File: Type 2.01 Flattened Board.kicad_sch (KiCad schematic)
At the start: 7 parts

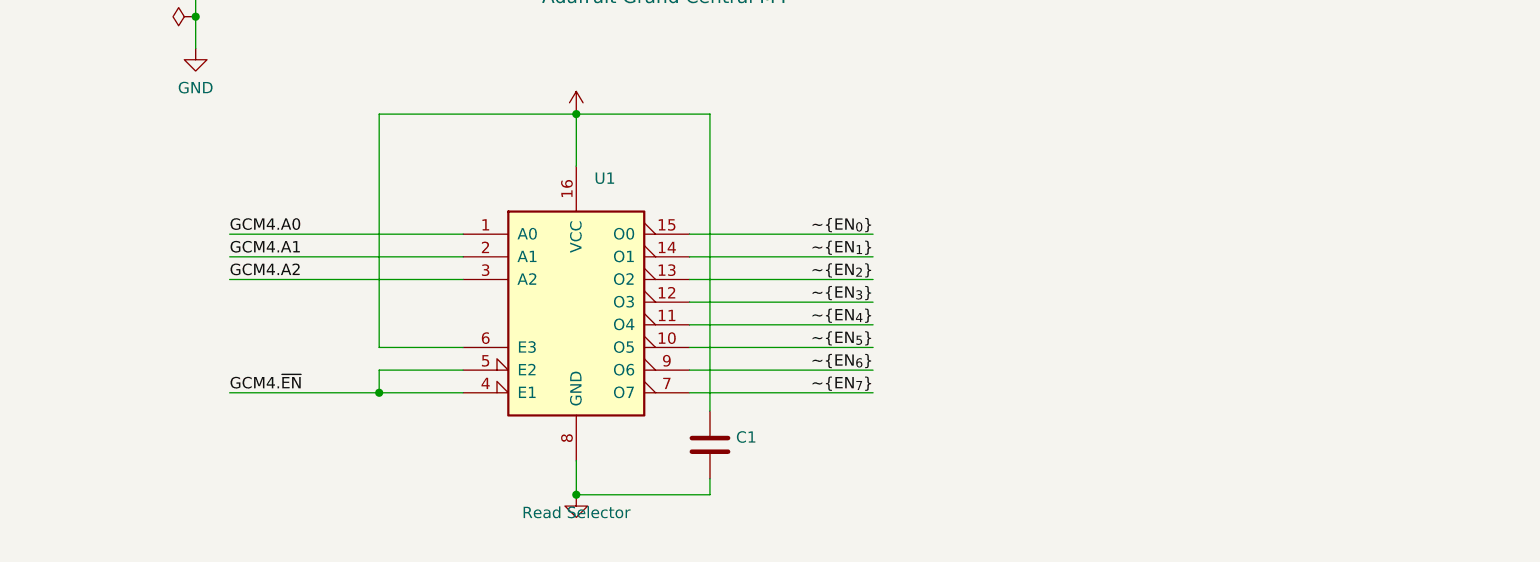
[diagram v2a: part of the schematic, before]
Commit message: Added the LOW global label
Simplify things
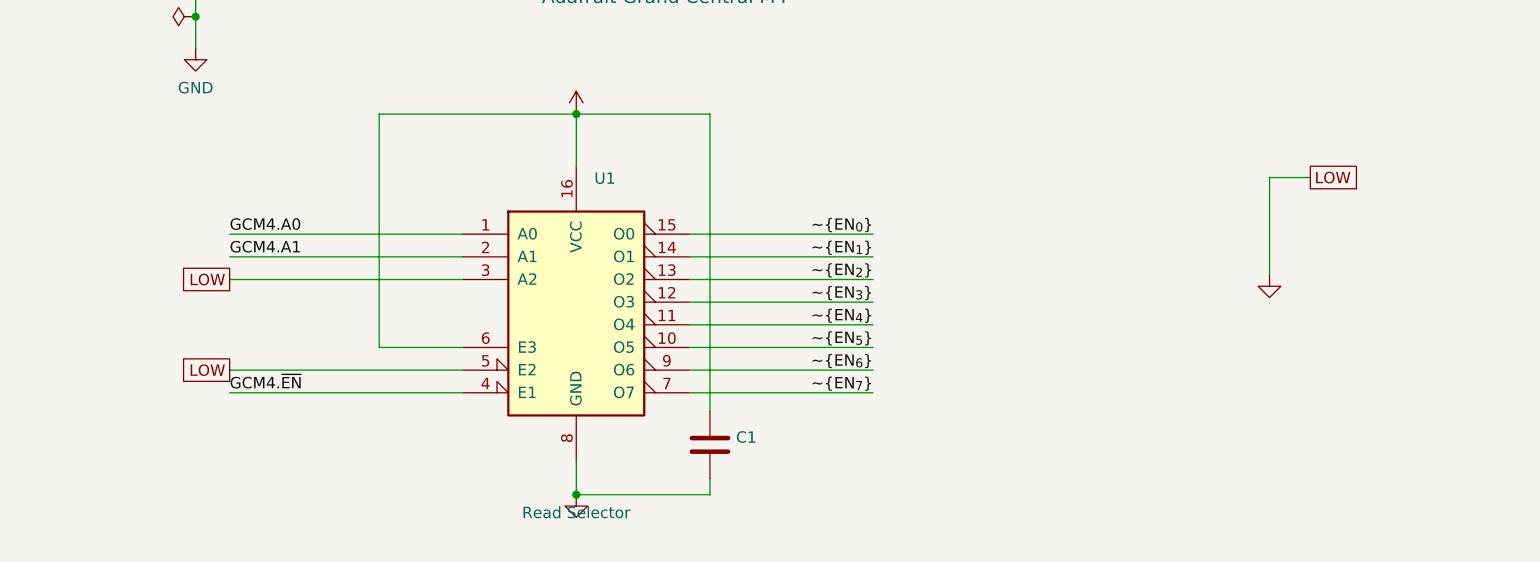
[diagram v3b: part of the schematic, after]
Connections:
- net GCM4.A2 is gone; now on net GND: U1.3 (A2)
- net BUS.PA23: no longer U1.5 (E2)
- net GND: now also U1.5 (E2)
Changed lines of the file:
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@@
   (junction (at 54.102 193.548) (diameter 0) (color 0 0 0 0)
   )
-  (junction (at 74.676 235.712) (diameter 0) (color 0 0 0 0)
-  )
   (junction (at 130.302 16.51) (diameter 0) (color 0 0 0 0)
   )
@@
     (stroke (width 0) (type default) (color 0 0 0 0))
   )
+  (wire (pts (xy 179.07 211.582) (xy 174.498 211.582))
+    (stroke (width 0) (type default) (color 0 0 0 0))
+  )
   (wire (pts (xy 139.7 159.512) (xy 187.452 159.512))
     (stroke (width 0) (type default) (color 0 0 0 0))
@@
     (stroke (width 0) (type default) (color 0 0 0 0))
   )
-  (wire (pts (xy 57.912 235.712) (xy 74.676 235.712))
+  (wire (pts (xy 174.498 211.582) (xy 174.498 222.504))
+    (stroke (width 0) (type default) (color 0 0 0 0))
+  )
+  (wire (pts (xy 57.912 235.712) (xy 84.074 235.712))
     (stroke (width 0) (type default) (color 0 0 0 0))
   )
@@
     (stroke (width 0) (type default) (color 0 0 0 0))
   )
-  (wire (pts (xy 84.074 233.172) (xy 74.676 233.172))
+  (wire (pts (xy 57.912 233.172) (xy 84.074 233.172))
     (stroke (width 0) (type default) (color 0 0 0 0))
   )
@@
     (stroke (width 0) (type default) (color 0 0 0 0))
   )
-  (wire (pts (xy 74.676 235.712) (xy 84.074 235.712))
-    (stroke (width 0) (type default) (color 0 0 0 0))
-  )
   (wire (pts (xy 84.074 230.632) (xy 74.676 230.632))
     (stroke (width 0) (type default) (color 0 0 0 0))
@@
     (stroke (width 0) (type default) (color 0 0 0 0))
   )
-  (wire (pts (xy 74.676 233.172) (xy 74.676 235.712))
-    (stroke (width 0) (type default) (color 0 0 0 0))
-  )
   (bus (pts (xy 313.436 181.61) (xy 313.436 160.274))
     (stroke (width 0) (type default) (color 0 0 0 0))
@@
     (effects (font (size 1.27 1.27)) (justify left bottom))
   )
-  (label "GCM4.A2" (at 57.912 223.012 0)
-    (effects (font (size 1.27 1.27)) (justify left bottom))
-  )
   (label "BUS.PA2" (at 61.214 106.172 0)
     (effects (font (size 1.27 1.27)) (justify left bottom))
@@
     (effects (font (size 1.27 1.27)) (justify right bottom))
   )
+  (global_label "LOW" (shape passive) (at 179.07 211.582 0) (fields_autoplaced)
+    (effects (font (size 1.27 1.27)) (justify left))
+    (property "Intersheet References" "${INTERSHEET_REFS}" (id 0) (at 185.2042 211.5026 0)
+      (effects (font (size 1.27 1.27)) (justify left) hide)
+    )
+  )
+  (global_label "LOW" (shape passive) (at 57.912 233.172 180) (fields_autoplaced)
+    (effects (font (size 1.27 1.27)) (justify right))
+    (property "Intersheet References" "${INTERSHEET_REFS}" (id 0) (at 51.7778 233.2514 0)
+      (effects (font (size 1.27 1.27)) (justify right) hide)
+    )
+  )
+  (global_label "LOW" (shape passive) (at 57.912 223.012 180) (fields_autoplaced)
+    (effects (font (size 1.27 1.27)) (justify right))
+    (property "Intersheet References" "${INTERSHEET_REFS}" (id 0) (at 51.7778 223.0914 0)
+      (effects (font (size 1.27 1.27)) (justify right) hide)
+    )
+  )
   (symbol (lib_id "power:VCC") (at 96.774 204.47 0) (unit 1)
     (in_bom yes) (on_board yes) (fields_autoplaced)
@@
     (pin "1")
   )
+  (symbol (lib_id "power:GND") (at 174.498 222.504 0) (unit 1)
+    (in_bom yes) (on_board yes) (fields_autoplaced)
+    (property "Reference" "#PWR?" (id 0) (at 174.498 228.854 0)
+      (effects (font (size 1.27 1.27)) hide)
+    )
+    (property "Value" "" (id 1) (at 174.498 226.9474 0))
+    (property "Footprint" "" (id 2) (at 174.498 222.504 0)
+      (effects (font (size 1.27 1.27)) hide)
+    )
+    (property "Datasheet" "" (id 3) (at 174.498 222.504 0)
+      (effects (font (size 1.27 1.27)) hide)
+    )
+    (pin "1")
+  )
   (symbol (lib_id "power:PWR_FLAG") (at 51.308 70.104 90) (unit 1)
     (in_bom yes) (on_board yes) (fields_autoplaced)
@@
       (reference "#FLG04") (unit 1) (value "PWR_FLAG") (footprint "")
     )
+    (path "/2d26b58a-1259-4cf5-aa8e-80f6b07f6859/dbaa682e-c216-48b7-8387-1a13814affa0"
+      (reference "#PWR01") (unit 1) (value "VCC") (footprint "")
+    )
+    (path "/2d26b58a-1259-4cf5-aa8e-80f6b07f6859/37c71bdd-f116-43fa-ad22-d47f0cad06e3"
+      (reference "#PWR02") (unit 1) (value "VCC") (footprint "")
+    )
+    (path "/2d26b58a-1259-4cf5-aa8e-80f6b07f6859/8f818677-5f2a-4233-a92b-47d4a000a4d4"
+      (reference "#PWR03") (unit 1) (value "GND") (footprint "")
+    )
+    (path "/2d26b58a-1259-4cf5-aa8e-80f6b07f6859/a685fc36-4bf3-4af6-ba0d-76e84fb6976e"
+      (reference "#PWR04") (unit 1) (value "GND") (footprint "")
+    )
+    (path "/cd4173d7-5549-43d9-b4b1-83989500a84c/eca025d3-1945-4a1c-930a-e419169f5e7e"
+      (reference "#PWR05") (unit 1) (value "+5V") (footprint "")
+    )
     (path "/14bf0462-80dc-4081-bb58-034085ad17f6"
       (reference "#PWR0101") (unit 1) (value "GND") (footprint "")
@@
       (reference "#PWR0183") (unit 1) (value "GND") (footprint "")
     )
-    (path "/2d26b58a-1259-4cf5-aa8e-80f6b07f6859/37c71bdd-f116-43fa-ad22-d47f0cad06e3"
-      (reference "#PWR?") (unit 1) (value "VCC") (footprint "")
-    )
-    (path "/2d26b58a-1259-4cf5-aa8e-80f6b07f6859/8f818677-5f2a-4233-a92b-47d4a000a4d4"
-      (reference "#PWR?") (unit 1) (value "GND") (footprint "")
-    )
-    (path "/2d26b58a-1259-4cf5-aa8e-80f6b07f6859/a685fc36-4bf3-4af6-ba0d-76e84fb6976e"
+    (path "/edbfded8-58b0-4c33-ba55-66a325a1b8e4"
       (reference "#PWR?") (unit 1) (value "GND") (footprint "")
     )
-    (path "/2d26b58a-1259-4cf5-aa8e-80f6b07f6859/dbaa682e-c216-48b7-8387-1a13814affa0"
-      (reference "#PWR?") (unit 1) (value "VCC") (footprint "")
-    )
-    (path "/cd4173d7-5549-43d9-b4b1-83989500a84c/eca025d3-1945-4a1c-930a-e419169f5e7e"
-      (reference "#PWR?") (unit 1) (value "+5V") (footprint "")
-    )
     (path "/843908a6-3a9c-4b81-8146-ddbddcf625df"
       (reference "C1") (unit 1) (value "C") (footprint "Capacitors_SMD:C_0805_HandSoldering")
@@
       (reference "C14") (unit 1) (value "C") (footprint "Capacitors_SMD:C_0805_HandSoldering")
     )
+    (path "/2d26b58a-1259-4cf5-aa8e-80f6b07f6859/b4574386-585f-44d1-a831-0eb6c71ebc11"
+      (reference "C15") (unit 1) (value "C") (footprint "")
+    )
     (path "/cd4173d7-5549-43d9-b4b1-83989500a84c/dd15c58d-5f76-4e11-988d-cb09d9458dfa"
       (reference "C16") (unit 1) (value "C") (footprint "Capacitors_SMD:C_0805_HandSoldering")
@@
       (reference "C37") (unit 1) (value "C") (footprint "Capacitors_SMD:C_0805_HandSoldering")
     )
-    (path "/2d26b58a-1259-4cf5-aa8e-80f6b07f6859/b4574386-585f-44d1-a831-0eb6c71ebc11"
-      (reference "C?") (unit 1) (value "C") (footprint "")
-    )
     (path "/2d26b58a-1259-4cf5-aa8e-80f6b07f6859/c1ae408c-8a4f-4105-a1e4-25705c794b80"
-      (reference "C?") (unit 1) (value "C") (footprint "")
+      (reference "C38") (unit 1) (value "C") (footprint "")
     )
     (path "/cd4173d7-5549-43d9-b4b1-83989500a84c/909ad6f6-fd1f-4fe0-baef-2369917a2988"
@@
       (reference "U11") (unit 1) (value "74AHC244") (footprint "Package_DIP:DIP-20_W7.62mm_Socket")
     )
+    (path "/2d26b58a-1259-4cf5-aa8e-80f6b07f6859/e7099e49-45b2-4d91-83f4-8a1a8eeecb05"
+      (reference "U12") (unit 1) (value "74HC244") (footprint "")
+    )
     (path "/cd4173d7-5549-43d9-b4b1-83989500a84c/4c98d838-4530-4c37-a157-b3a85ef63936"
       (reference "U13") (unit 1) (value "74AHC04") (footprint "Package_DIP:DIP-14_W7.62mm_Socket")
@@
     )
     (path "/2d26b58a-1259-4cf5-aa8e-80f6b07f6859/c58d427c-aec3-48b4-915f-b936c8e35e2f"
-      (reference "U?") (unit 1) (value "74HC244") (footprint "")
-    )
-    (path "/2d26b58a-1259-4cf5-aa8e-80f6b07f6859/e7099e49-45b2-4d91-83f4-8a1a8eeecb05"
-      (reference "U?") (unit 1) (value "74HC244") (footprint "")
+      (reference "U21") (unit 1) (value "74HC244") (footprint "")
     )
     (path "/2bd6b25f-a519-4224-8dd9-2e42d262ce2e"

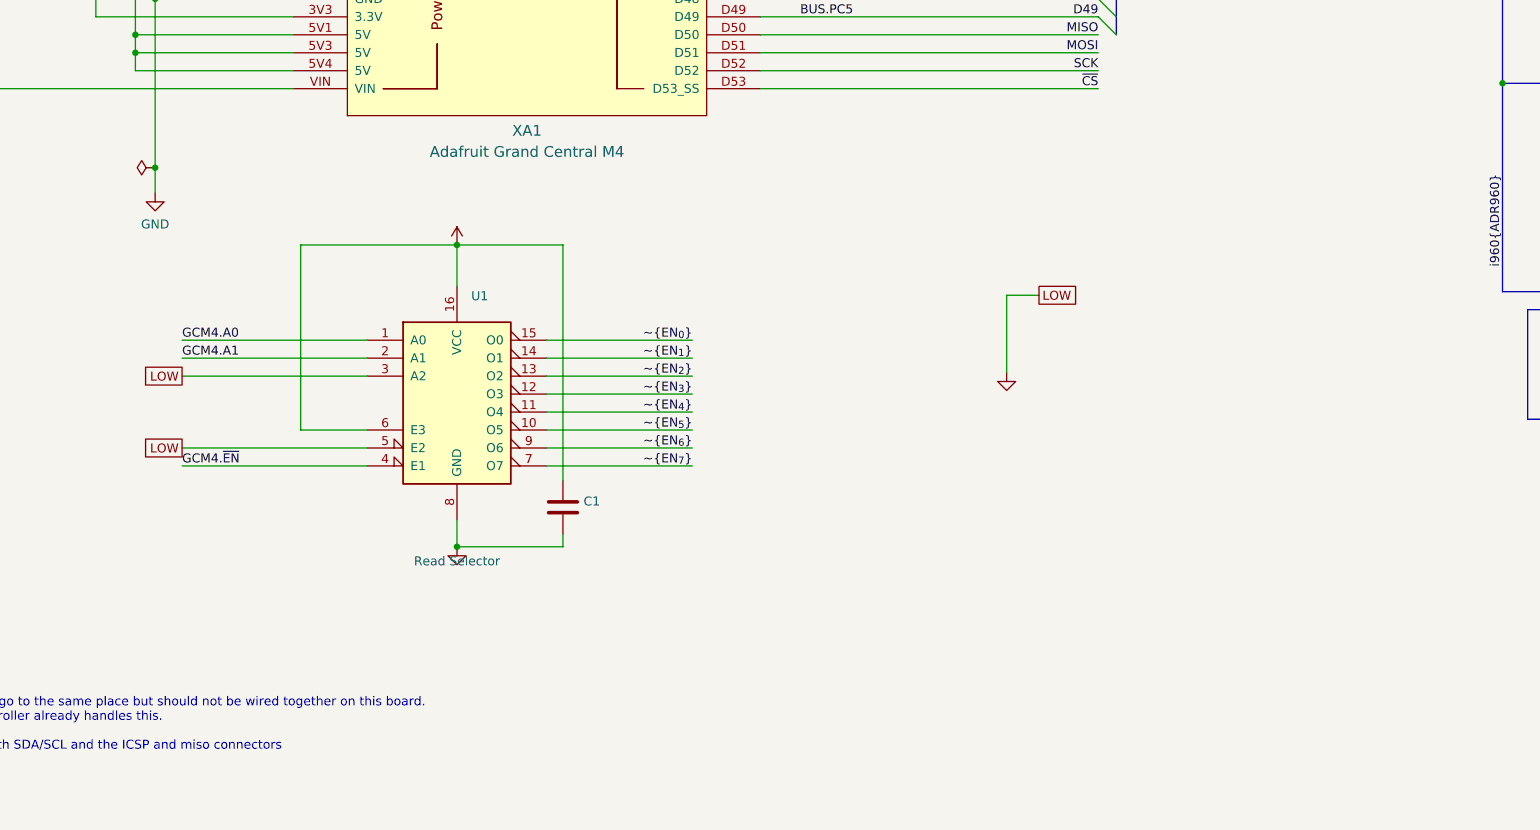
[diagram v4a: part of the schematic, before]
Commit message: Initial layout but I think I can use AHC157s to assist in device selection
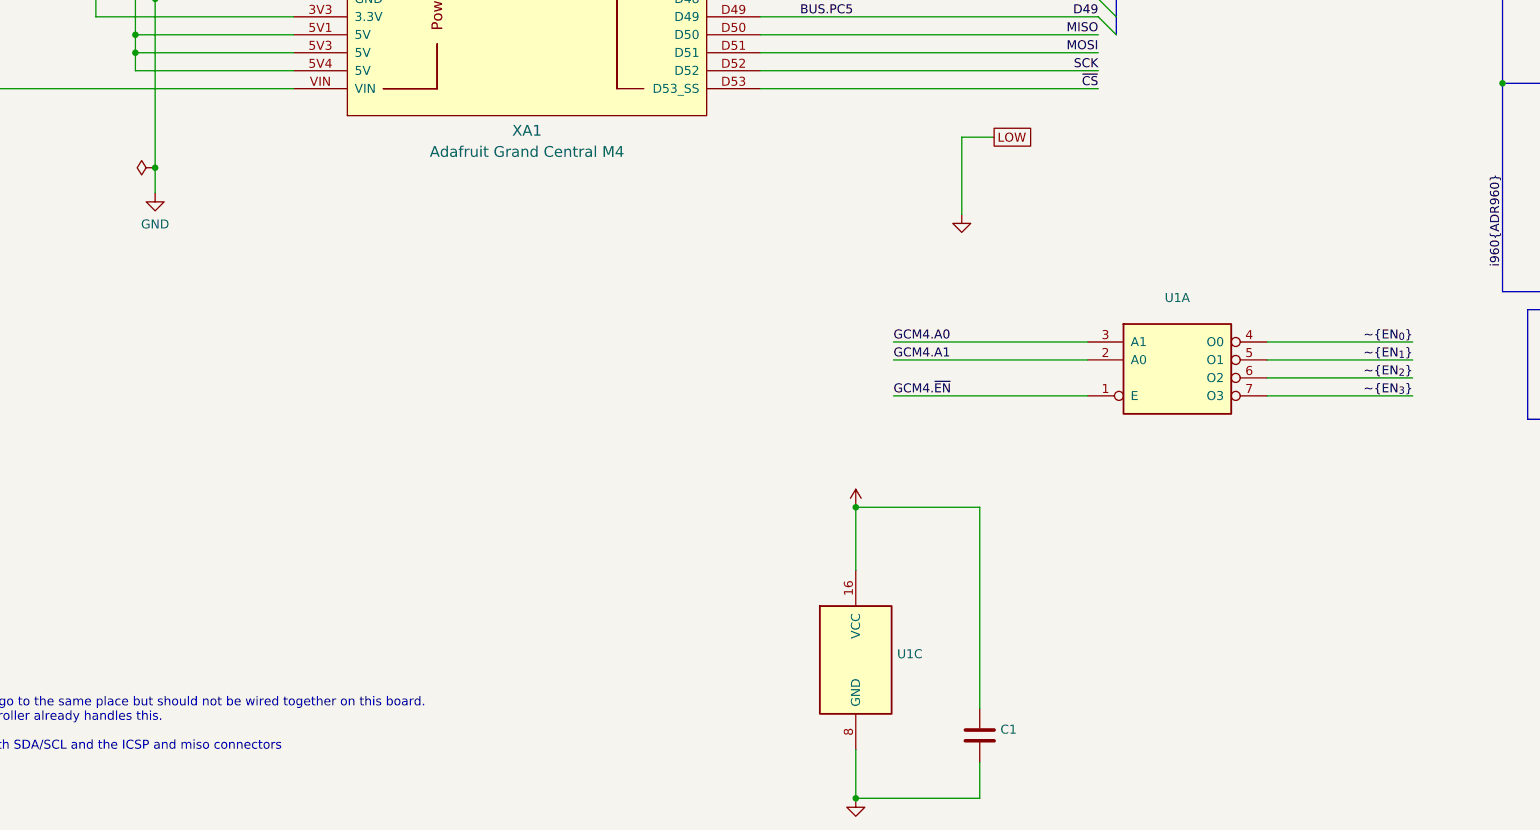
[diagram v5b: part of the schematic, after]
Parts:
- removed U1: (no value), symbol 74xx:74LS138
- added U1: (no value), symbol 74xx:74LS139
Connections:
- net BUS.PA21: now also U1.3 (A1)
- net BUS.PA22: now also U1.2 (A0)
- net BUS.PA23: now also U1.1 (E)
- net GND: now also U1.8 (GND)
- net VCC: now also U1.16 (VCC)
- net ~{EN_{0}}: now also U1.4 (O0)
- net ~{EN_{1}}: now also U1.5 (O1)
- net ~{EN_{2}}: now also U1.6 (O2)
- net ~{EN_{3}}: now also U1.7 (O3)
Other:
- moved on the sheet: C1
